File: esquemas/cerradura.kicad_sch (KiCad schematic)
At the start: 11 parts, among them J1 Conn_02x20_Odd_Even, J11 2n2222, J13 bornes_motor, J14 bornes_buzzer, J2 Conn_02x20_Odd_Even, J4 num_keypad, J6 R305_sensor, J7 RC522_sensor, J8 ssd1306_dsp, U1 ESP32_c3_mini

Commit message: arreglo comentario
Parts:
- removed J11: 2n2222, Connector_PinHeader_2.54mm:PinHeader_1x03_P2.54mm_Vertical, symbol Connector:Conn_01x03_Socket
- added Q1: PN2222A, Package_TO_SOT_THT:TO-92_Inline, symbol Transistor_BJT:PN2222A
- added R1: 10K, symbol Device:R
- added U2: A1104xLH, Package_TO_SOT_SMD:SOT-23W, symbol Sensor_Magnetic:A1104xLH
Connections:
- net +3.3V: now also R1.1
- net +5V: now also U2.1 (V_{CC})
- net GND: now also Q1.1 (E), U2.3 (GND)
- net buzzer_sgn: now also Q1.2 (B)
- net at J14.2 (Pin_2): now also Q1.3 (C)
- net door_sensor: now reaches J1.36 (Pin_36)
- net door_sensor: now also R1.2, U2.2 (V_{OUT})
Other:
- moved on the sheet: A1, J13, J14, J4, U1

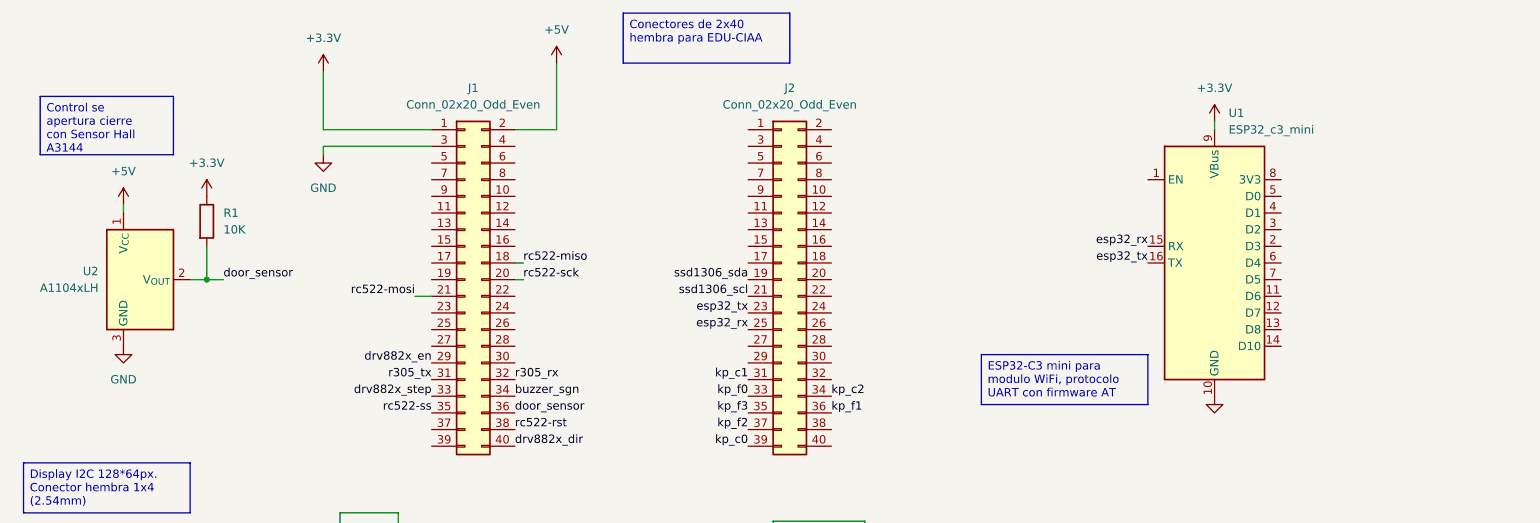
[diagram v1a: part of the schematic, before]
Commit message: cambio socket esp
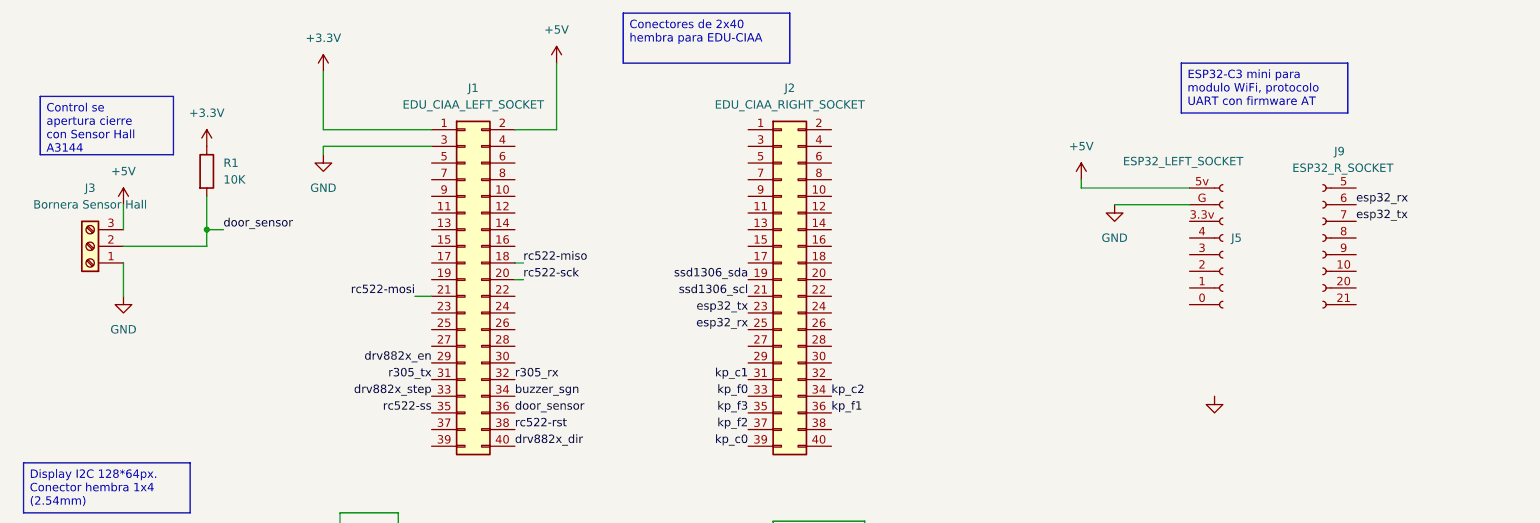
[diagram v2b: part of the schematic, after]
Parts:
- removed U1: ESP32_c3_mini, RF_Module:WEMOS_C3_mini, symbol RF_Module:WEMOS_C3_mini
- removed U2: A1104xLH, Package_TO_SOT_SMD:SOT-23W, symbol Sensor_Magnetic:A1104xLH
- added J3: Bornera Sensor Hall, TerminalBlock:TerminalBlock_Altech_AK300-3_P5.00mm, symbol Connector:Screw_Terminal_01x03
- added J5: ESP32_LEFT_SOCKET, Connector_Molex:Molex_KK-254_AE-6410-08A_1x08_P2.54mm_Vertical, symbol Connector:Conn_01x08_Socket
- added J9: ESP32_R_SOCKET, symbol Connector:Conn_01x08_Socket
- J1: value Conn_02x20_Odd_Even -> EDU_CIAA_LEFT_SOCKET
- J2: value Conn_02x20_Odd_Even -> EDU_CIAA_RIGHT_SOCKET
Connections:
- net +5V: now also J3.3 (Pin_3), J5.5v
- net GND: now also J3.1 (Pin_1), J5.G
- net door_sensor: now also J3.2 (Pin_2)
- net esp32_rx: now also J9.6 (Pin_6)
- net esp32_tx: now also J9.7 (Pin_7)
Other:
- moved on the sheet: R1

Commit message: entrada 12v
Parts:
- added J10: HW-677 DC-DC, Connector_PinHeader_2.00mm:PinHeader_2x02_P2.00mm_Vertical_SMD, symbol Connector_Generic:Conn_02x02_Counter_Clockwise
- added J11: Jack-DC, Connector_BarrelJack:BarrelJack_SwitchcraftConxall_RAPC10U_Horizontal, symbol Connector:Jack-DC
- added J12: brones_5v, TerminalBlock:TerminalBlock_Altech_AK300-2_P5.00mm, symbol Connector:Screw_Terminal_01x02
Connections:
- net +3.3V: no longer A1.13 (~{RST}), A1.14 (~{SLP})
- net +5V: no longer J5.5v
- net GND: no longer A1.1 (GND), A1.7 (GND), J5.G
- net +3.3Vp2: now reaches J2.1 (Pin_1)
- net +3.3Vp2: now also A1.13 (~{RST}), A1.14 (~{SLP})
- net +5Vp2: now reaches J2.2 (Pin_2)
- net +5Vp2: now also J5.5v
- net GNDp2: now reaches J2.3 (Pin_3)
- net GNDp2: now also A1.1 (GND), J5.G
- new net: J10.out+ (4), J12.1 (Pin_1)
- new net: J10.out- (3), J12.2 (Pin_2)
- new net +12V: J10.in+ (Pin_1), J11.1
- new net GND-12: J10.in- (Pin_2), J11.2
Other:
- moved on the sheet: J5, J9

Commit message: entrega 1
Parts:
- J10: value HW-677 DC-DC -> lm2596hvs DC-DC
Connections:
- net rc522-irq: now also J1.28 (Pin_28)
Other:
- moved on the sheet: J10, J11, J12, J5, J9

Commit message: avace pcb
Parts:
- 10K1: renamed from R1; footprint (none) -> Resistor_SMD:R_2010_5025Metric
- 5V_BORN1: renamed from J12; value brones_5v -> bornes_5v
- ESP_L1: renamed from J9; value ESP32_R_SOCKET -> ESP32_LEFT_SOCKET; footprint (none) -> Connector_Molex:Molex_KK-254_AE-6410-08A_1x08_P2.54mm_Vertical
- ESP_R1: renamed from J5; value ESP32_LEFT_SOCKET -> ESP32_RIGHT_SOCKET
- renumbered J11 to 12V-BORN1, J3 to A3144, J14 to BUZZER1, A1 to DRV8825, J1 to EDU_L1, J2 to EDU_R1, J4 to Keypad1, J10 to LV2596HVS1, J13 to MOTOR_BORN1, J6 to R305, J7 to RC522, J8 to SSD1306
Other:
- note added: "Cerradura electronica Grupo 6 Taller de proyectos I UNLP"
- note added: "v0.0.1"
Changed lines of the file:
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@@
 	(generator_version "9.0")
 	(paper "A4")
+	(text "v0.0.1"
+		(exclude_from_sim no)
+		(at 272.034 193.294 0)
+		(effects
+			(font
+				(size 1.27 1.27)
+			)
+		)
+	)
+	(text "Cerradura electronica Grupo 6 Taller de proyectos I UNLP"
+		(exclude_from_sim no)
+		(at 215.392 189.992 0)
+		(effects
+			(font
+				(size 1.27 1.27)
+			)
+		)
+	)
 	(text_box "Driver de motor paso a paso DRV8825 con bornera."
 		(exclude_from_sim no)
@@
 		(on_board yes)
 		(dnp no)
-		(property "Reference" "J5"
-			(at 213.36 62.2299 0)
+		(property "Reference" "ESP_R1"
+			(at 217.424 48.768 0)
 			(effects
 				(font
@@
 			)
 		)
-		(property "Value" "ESP32_LEFT_SOCKET"
-			(at 229.87 50.546 0)
+		(property "Value" "ESP32_RIGHT_SOCKET"
+			(at 229.362 51.562 0)
 			(effects
 				(font
@@
 			(project ""
 				(path "/5ec40689-7e61-4c5f-9022-56a5e47f7bec"
-					(reference "J5")
+					(reference "ESP_R1")
 					(unit 1)
 				)
@@
 		(on_board yes)
 		(dnp no)
-		(property "Reference" "J6"
+		(property "Reference" "R305"
 			(at 77.47 133.35 90)
 			(effects
@@
 			(project ""
 				(path "/5ec40689-7e61-4c5f-9022-56a5e47f7bec"
-					(reference "J6")
+					(reference "R305")
 					(unit 1)
 				)
@@
 		(dnp no)
 		(fields_autoplaced yes)
-		(property "Reference" "J2"
+		(property "Reference" "EDU_R1"
 			(at 135.89 46.99 0)
 			(effects
@@
 			(project "cerradura"
 				(path "/5ec40689-7e61-4c5f-9022-56a5e47f7bec"
-					(reference "J2")
+					(reference "EDU_R1")
 					(unit 1)
 				)
@@
 		(dnp no)
 		(fields_autoplaced yes)
-		(property "Reference" "A1"
+		(property "Reference" "DRV8825"
 			(at 209.1533 120.65 0)
 			(effects
@@
 			(project ""
 				(path "/5ec40689-7e61-4c5f-9022-56a5e47f7bec"
-					(reference "A1")
+					(reference "DRV8825")
 					(unit 1)
 				)
@@
 		(dnp no)
 		(fields_autoplaced yes)
-		(property "Reference" "J11"
+		(property "Reference" "12V-BORN1"
 			(at 187.96 86.36 0)
 			(effects
@@
 			(project ""
 				(path "/5ec40689-7e61-4c5f-9022-56a5e47f7bec"
-					(reference "J11")
+					(reference "12V-BORN1")
 					(unit 1)
 				)
@@
 		(on_board yes)
 		(dnp no)
-		(property "Reference" "J9"
+		(property "Reference" "ESP_L1"
 			(at 199.39 49.022 0)
 			(effects
@@
 			)
 		)
-		(property "Value" "ESP32_R_SOCKET"
-			(at 198.882 51.562 0)
+		(property "Value" "ESP32_LEFT_SOCKET"
+			(at 196.596 51.562 0)
 			(effects
 				(font
@@
 			)
 		)
-		(property "Footprint" ""
+		(property "Footprint" "Connector_Molex:Molex_KK-254_AE-6410-08A_1x08_P2.54mm_Vertical"
 			(at 201.93 62.23 0)
 			(effects
@@
 			(project ""
 				(path "/5ec40689-7e61-4c5f-9022-56a5e47f7bec"
-					(reference "J9")
+					(reference "ESP_L1")
 					(unit 1)
 				)
@@
 		(on_board yes)
 		(dnp no)
-		(property "Reference" "J10"
+		(property "Reference" "LV2596HVS1"
 			(at 220.98 87.63 0)
 			(effects
@@
 			(project ""
 				(path "/5ec40689-7e61-4c5f-9022-56a5e47f7bec"
-					(reference "J10")
+					(reference "LV2596HVS1")
 					(unit 1)
 				)
@@
 		(dnp no)
 		(fields_autoplaced yes)
-		(property "Reference" "J3"
+		(property "Reference" "A3144"
 			(at 29.21 62.23 0)
 			(effects
@@
 			(project ""
 				(path "/5ec40689-7e61-4c5f-9022-56a5e47f7bec"
-					(reference "J3")
+					(reference "A3144")
 					(unit 1)
 				)
@@
 		(dnp no)
 		(fields_autoplaced yes)
-		(property "Reference" "J13"
+		(property "Reference" "MOTOR_BORN1"
 			(at 255.27 140.9699 0)
 			(effects
@@
 			(project ""
 				(path "/5ec40689-7e61-4c5f-9022-56a5e47f7bec"
-					(reference "J13")
+					(reference "MOTOR_BORN1")
 					(unit 1)
 				)
@@
 		(on_board yes)
 		(dnp no)
-		(property "Reference" "J4"
+		(property "Reference" "Keypad1"
 			(at 107.95 133.35 90)
 			(effects
@@
 			(project ""
 				(path "/5ec40689-7e61-4c5f-9022-56a5e47f7bec"
-					(reference "J4")
+					(reference "Keypad1")
 					(unit 1)
 				)
@@
 		(dnp no)
 		(fields_autoplaced yes)
-		(property "Reference" "R1"
+		(property "Reference" "10K1"
 			(at 49.53 58.4199 0)
 			(effects
@@
 			)
 		)
-		(property "Footprint" ""
+		(property "Footprint" "Resistor_SMD:R_2010_5025Metric"
 			(at 45.212 59.69 90)
 			(effects
@@
 			(project ""
 				(path "/5ec40689-7e61-4c5f-9022-56a5e47f7bec"
-					(reference "R1")
+					(reference "10K1")
 					(unit 1)
 				)
@@
 		(dnp no)
 		(fields_autoplaced yes)
-		(property "Reference" "J1"
+		(property "Reference" "EDU_L1"
 			(at 87.63 46.99 0)
 			(effects
@@
 			(project ""
 				(path "/5ec40689-7e61-4c5f-9022-56a5e47f7bec"
-					(reference "J1")
+					(reference "EDU_L1")
 					(unit 1)
 				)
@@
 		(on_board yes)
 		(dnp no)
-		(property "Reference" "J8"
+		(property "Reference" "SSD1306"
 			(at 50.8 119.3799 0)
 			(effects
@@
 			(project ""
 				(path "/5ec40689-7e61-4c5f-9022-56a5e47f7bec"
-					(reference "J8")
+					(reference "SSD1306")
 					(unit 1)
 				)
@@
 		(dnp no)
 		(fields_autoplaced yes)
-		(property "Reference" "J12"
+		(property "Reference" "5V_BORN1"
 			(at 240.03 93.9799 0)
 			(effects
@@
 			)
 		)
-		(property "Value" "brones_5v"
+		(property "Value" "bornes_5v"
 			(at 240.03 96.5199 0)
 			(effects
@@
 			(project "cerradura"
 				(path "/5ec40689-7e61-4c5f-9022-56a5e47f7bec"
-					(reference "J12")
+					(reference "5V_BORN1")
 					(unit 1)
 				)
@@
 		(on_board yes)
 		(dnp no)
-		(property "Reference" "J7"
+		(property "Reference" "RC522"
 			(at 151.13 137.16 90)
 			(effects
@@
 			(project "cerradura"
 				(path "/5ec40689-7e61-4c5f-9022-56a5e47f7bec"
-					(reference "J7")
+					(reference "RC522")
 					(unit 1)
 				)
@@
 		(dnp no)
 		(fields_autoplaced yes)
-		(property "Reference" "J14"
+		(property "Reference" "BUZZER1"
 			(at 55.88 163.8299 0)
 			(effects
@@
 			(project ""
 				(path "/5ec40689-7e61-4c5f-9022-56a5e47f7bec"
-					(reference "J14")
+					(reference "BUZZER1")
 					(unit 1)
 				)
